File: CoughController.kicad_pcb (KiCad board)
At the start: 2 copper layers, 99 x 85 mm, 50 parts, among them J3 AUDIO IN/OUT, J4 DIO-2, J5 GPIO-OUT, J6 GPIO-IN, K1 G6A-274P-ST-US DC12, K2 G6A-274P-ST-US DC12, U1 TLP627-2, U2 TLP627-2, U3 TLP627-2, U4 TLP627-2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

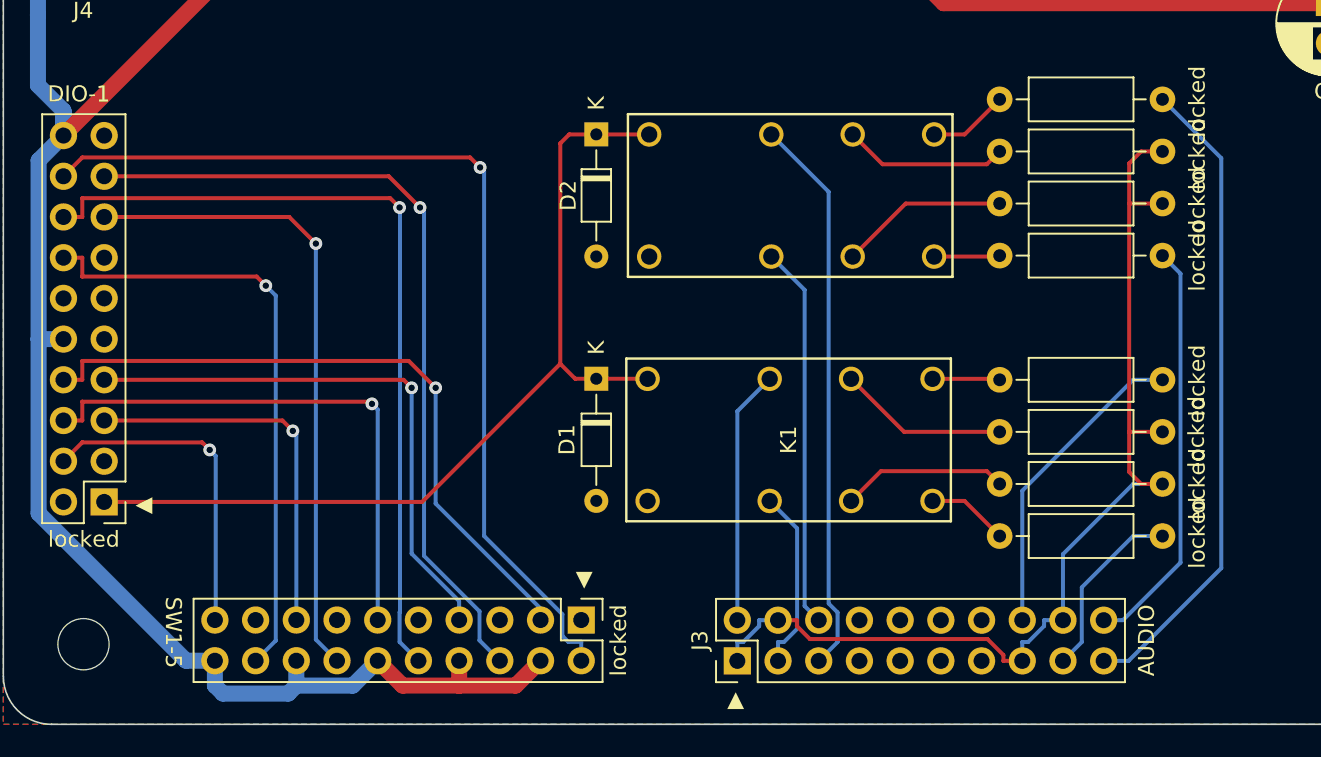
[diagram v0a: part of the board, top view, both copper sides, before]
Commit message: オーディオ線強化
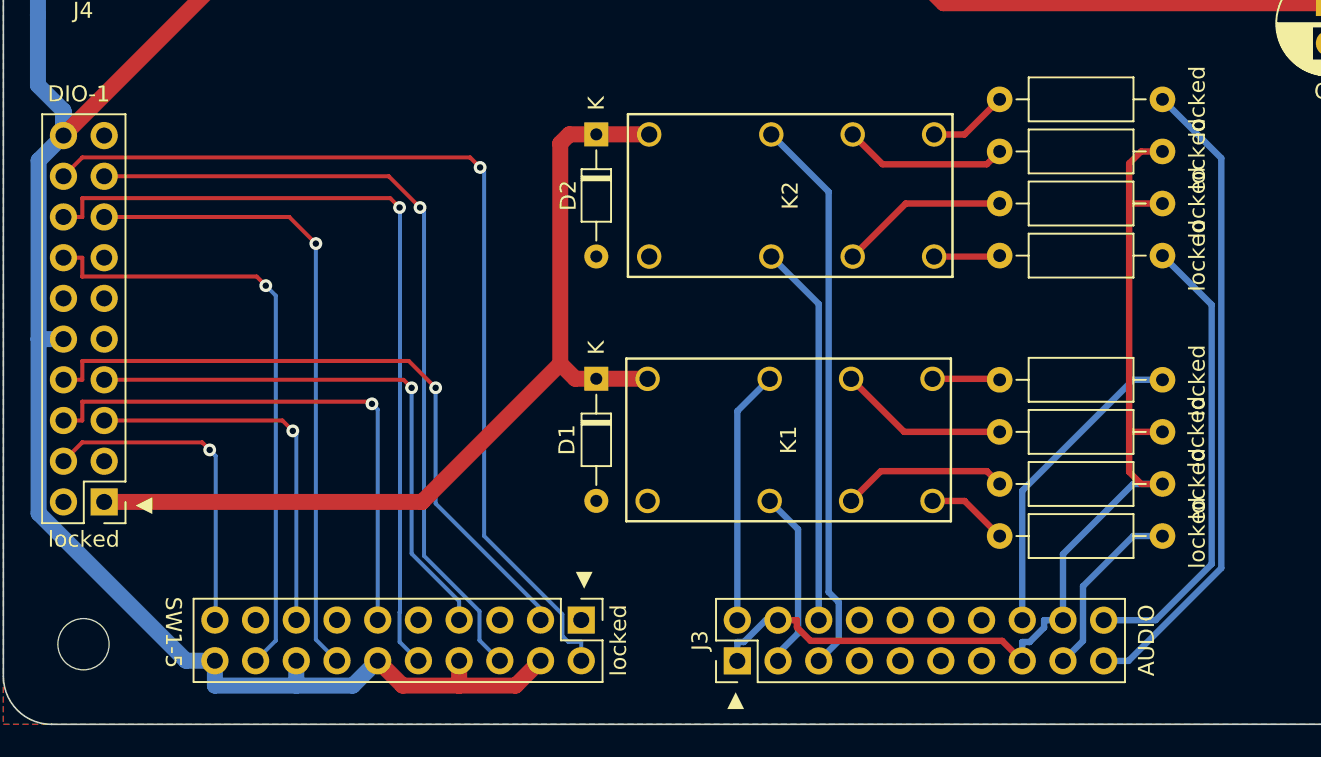
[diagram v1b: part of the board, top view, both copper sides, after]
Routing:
- net AUDIO-OUT-R-COLD: track 25.9 -> 28.7 mm

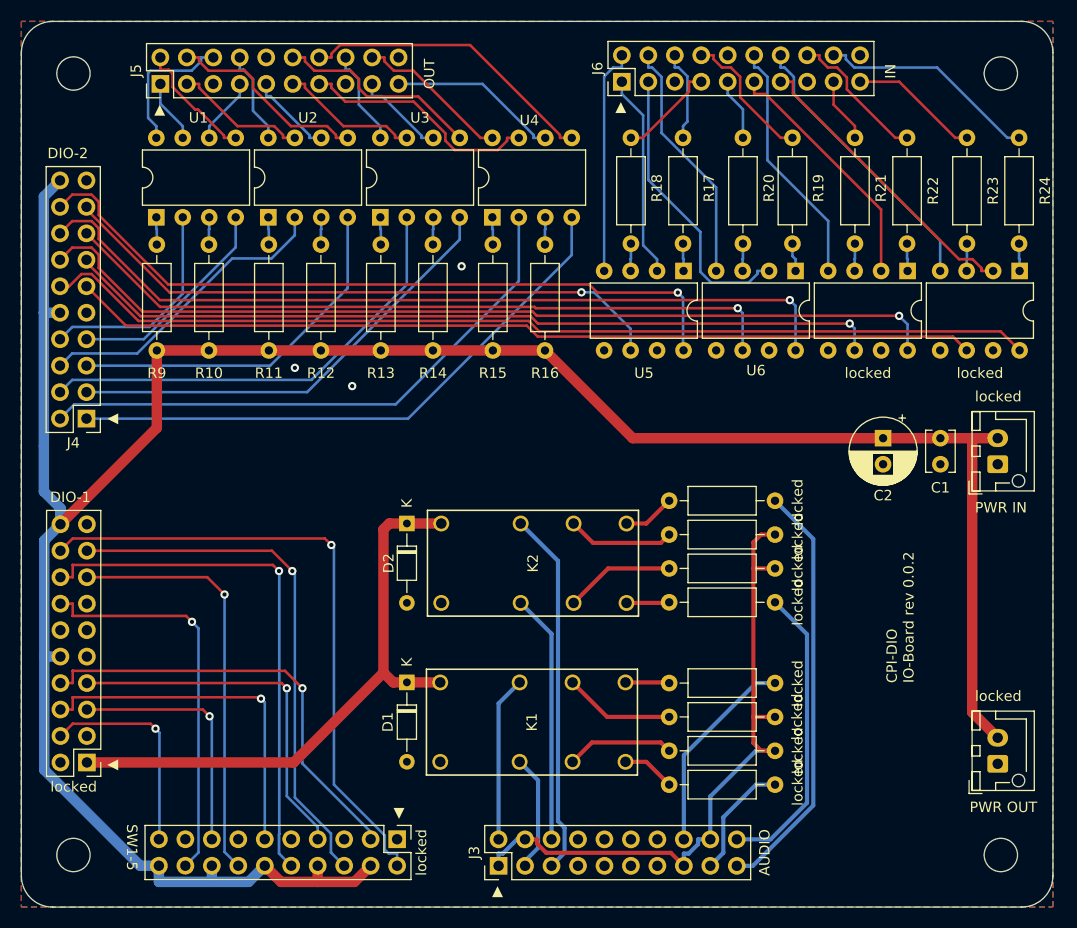
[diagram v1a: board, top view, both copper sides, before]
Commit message: リレー ロジックミス修正
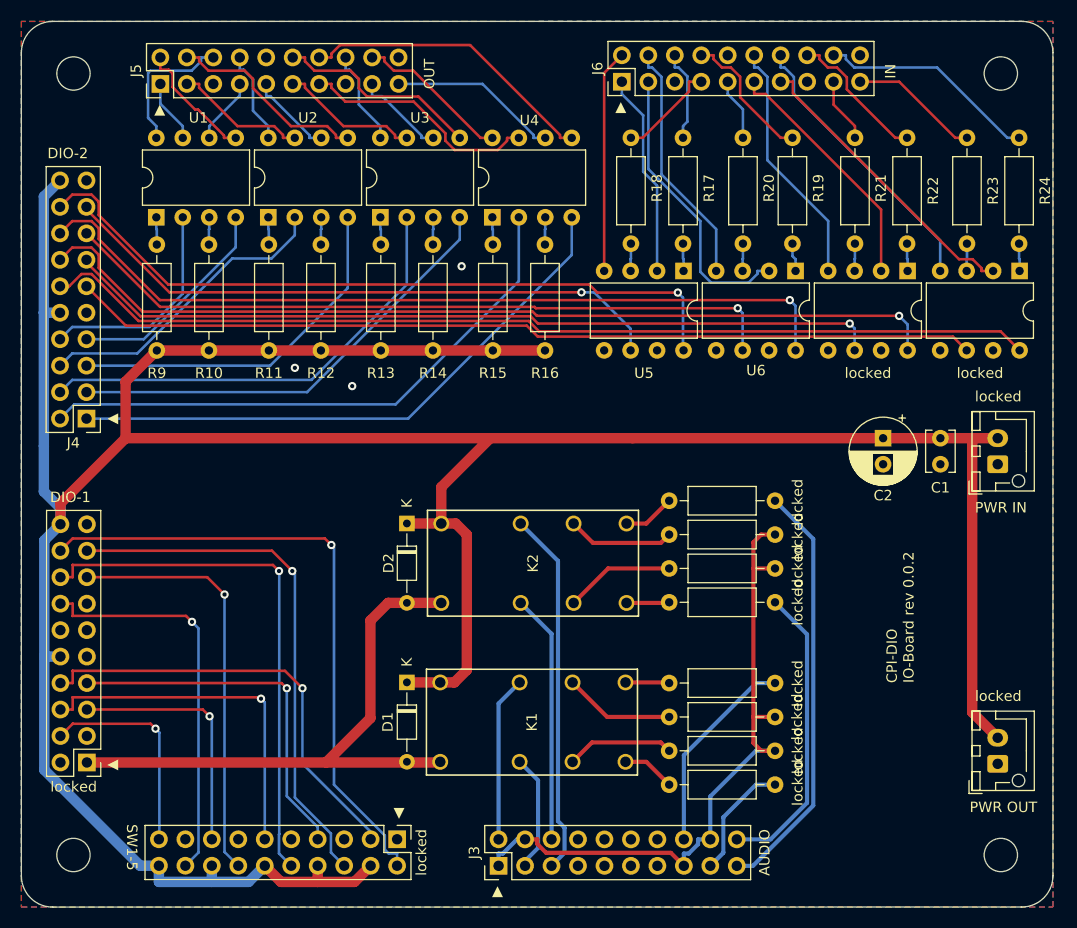
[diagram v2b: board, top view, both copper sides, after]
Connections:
- D1 pad 1: RY_POW -> COM0
- D1 pad 2: MCOM1 -> RY_POW
- D2 pad 1: RY_POW -> COM0
- D2 pad 2: MCOM1 -> RY_POW
- K1 pad 1: RY_POW -> COM0
- K1 pad 16: MCOM1 -> RY_POW
- K2 pad 1: RY_POW -> COM0
- K2 pad 16: MCOM1 -> RY_POW
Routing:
- net COM0: track 239.3 -> 311.6 mm
- net RY_POW: track 57.4 -> 56.8 mm

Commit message: AUDIO ソケット位置調整
ソケットピンヘッダが干渉するので移動
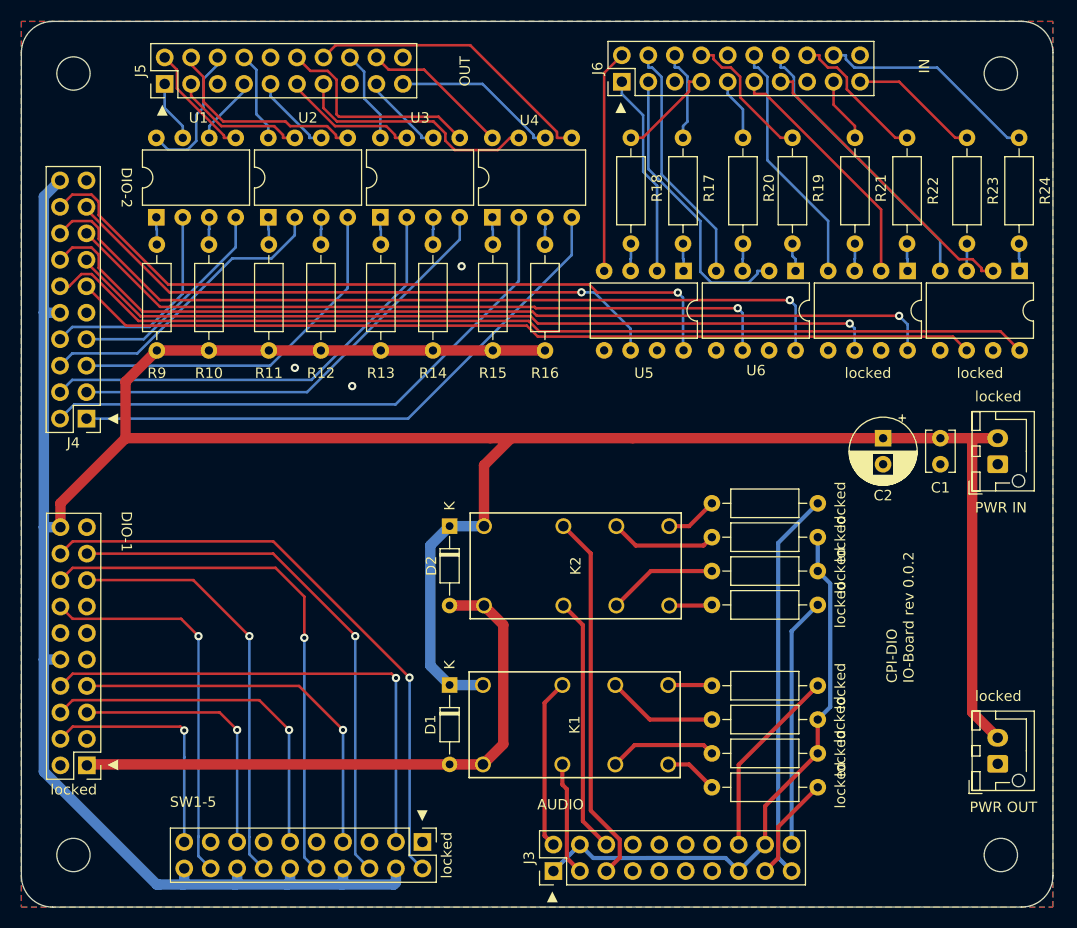
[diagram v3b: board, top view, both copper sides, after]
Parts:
- J3, J4, J5, J6, locked (x2): footprint Connector_PinHeader_2.54mm:PinHeader_2x10_P2.54mm_Vertical -> BoxHeader:BoxHeader_2x10_P2.54mm_Vertical
- moved J3 5.28 mm to (101.1, 146.5)
- moved K1 4.11 mm to (111.9, 128.7)
- moved locked 4.11 mm to (126.4, 114.5)
- moved locked 4.11 mm to (126.4, 111.2)
- moved locked 4.11 mm to (126.4, 138.5)
- moved locked 4.11 mm to (126.4, 132.0)
- moved D1 4.11 mm to (91.1, 128.7)
- moved D2 4.11 mm to (91.1, 113.4)
- moved K2 4.11 mm to (112.0, 113.4)
- moved locked 4.11 mm to (116.3, 128.8)
- moved locked 4.11 mm to (116.3, 135.2)
- moved locked 4.11 mm to (116.3, 117.8)
- moved locked 4.11 mm to (116.3, 121.0)
- moved locked 2.44 mm to (88.5, 143.8)
- moved J5 0.41 mm to (63.8, 71.0)
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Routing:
- net AUDIO-IN-L-GND: track 65.7 -> 56.1 mm
- net SW1/L1: track 42.3 -> 48.6 mm
- net AUDIO-OUT-R-COLD: track 28.7 -> 24.0 mm
- net AUDIO-OUT-R-HOT: track 40.5 -> 37.4 mm
- net SW5/L1: track 20.5 -> 23.2 mm
- net SW1/O: track 60.6 -> 58.2 mm
- net SW2/L1: track 35.1 -> 37.1 mm
- net SW4/L1: track 23.9 -> 25.9 mm
- net RY_POW: track 56.8 -> 58.2 mm
- net AUDIO-OUT-L-HOT: track 19.7 -> 18.4 mm
- net AUDIO-OUT-L-COLD: track 11.4 -> 10.1 mm
- net SW2/O: track 50.9 -> 51.9 mm
- net SW5/O: track 38.2 -> 37.2 mm
- net COM0: track 311.6 -> 312.7 mm
- net GPIO-OUT/2M: track 12.0 -> 11.2 mm
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
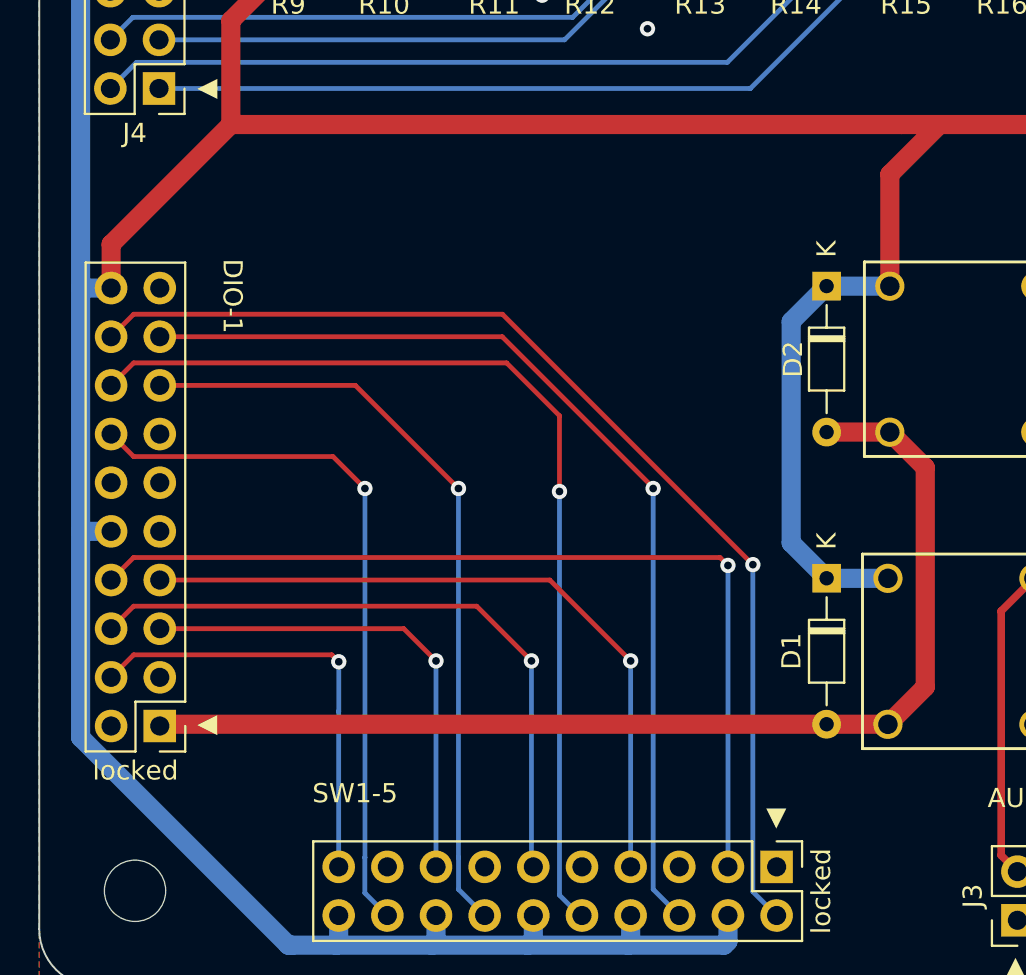
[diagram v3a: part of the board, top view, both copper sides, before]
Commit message: SW6/SW7を追加
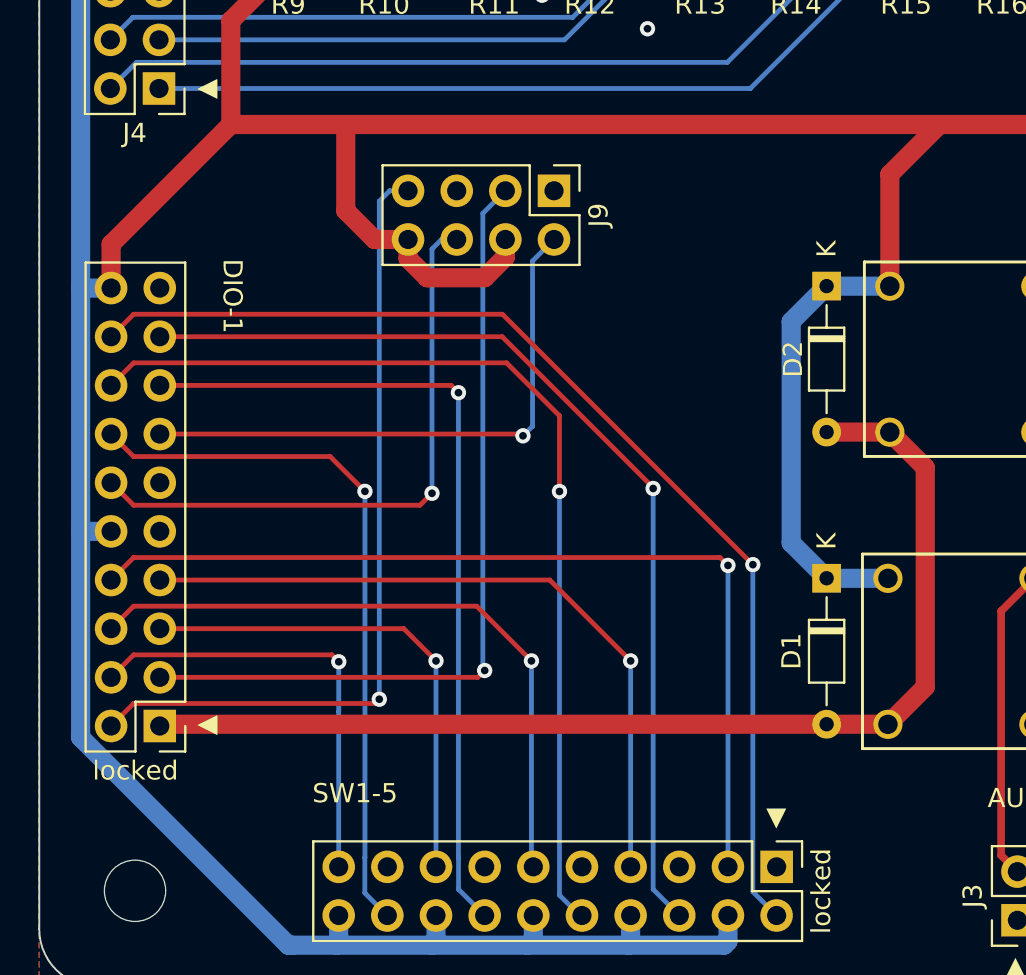
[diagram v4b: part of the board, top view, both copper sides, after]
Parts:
- added J9: Conn_02x04_Odd_Even, Connector_PinHeader_2.54mm:PinHeader_2x04_P2.54mm_Vertical, F.Cu at (76.9, 108.5)
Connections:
- locked pad 12: unconnected-(J2-Pin_12-Pad12) -> SW7/O
- locked pad 13: unconnected-(J2-Pin_13-Pad13) -> SW6/O
- locked pad 2: unconnected-(J2-Pin_2-Pad2) -> SW7/L1
- locked pad 3: unconnected-(J2-Pin_3-Pad3) -> SW6/L1
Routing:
- net SW6/L1: track 0.00 -> 42.7 mm, vias 0 -> 1
- net SW7/L1: track 0.00 -> 42.3 mm, vias 0 -> 1
- net SW7/O: track 0.00 -> 31.7 mm, vias 0 -> 1
- net SW6/O: track 0.00 -> 29.9 mm, vias 0 -> 1
- net COM0: track 312.7 -> 328.9 mm
- net SW4/O: track 40.7 -> 43.6 mm
